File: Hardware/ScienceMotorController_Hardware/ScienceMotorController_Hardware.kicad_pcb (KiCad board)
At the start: 2 copper layers, 124.5 x 104.9 mm, 109 parts, among them SW1 SW_Push, SW2 SW_Push, SW3 SW_Push, SW4 SW_Push, U1 TM4C129E_Launchpad, U2 3.3V OKI, U3 5V OKI, U4 VNH5019A_E, U5 VNH5019A_E, U6 VNH5019A_E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

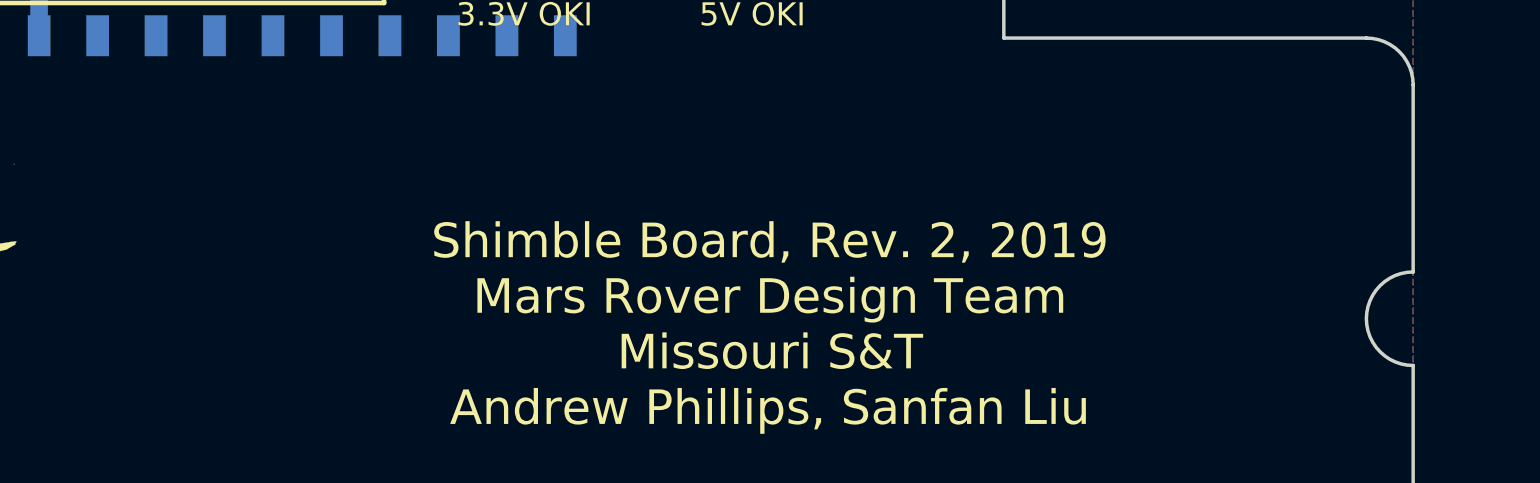
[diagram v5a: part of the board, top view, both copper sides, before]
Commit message: Fixed Silkscreen
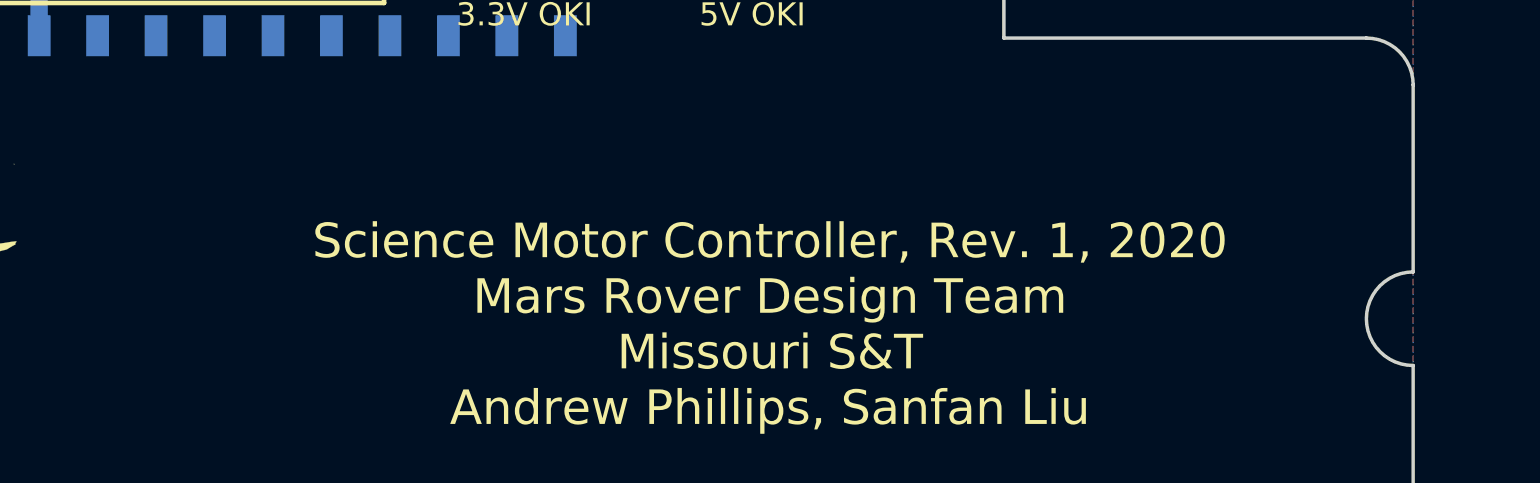
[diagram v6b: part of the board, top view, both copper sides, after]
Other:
- board text added: "Science Motor Controller, Rev. 1, 2020 Mars Rover Design Team Missouri S&T Andrew Phillips, Sanfan Liu"
- board text removed: "Shimble Board, Rev. 2, 2019 Mars Rover Design Team Missouri S&T Andrew Phillips, Sanfan Liu"

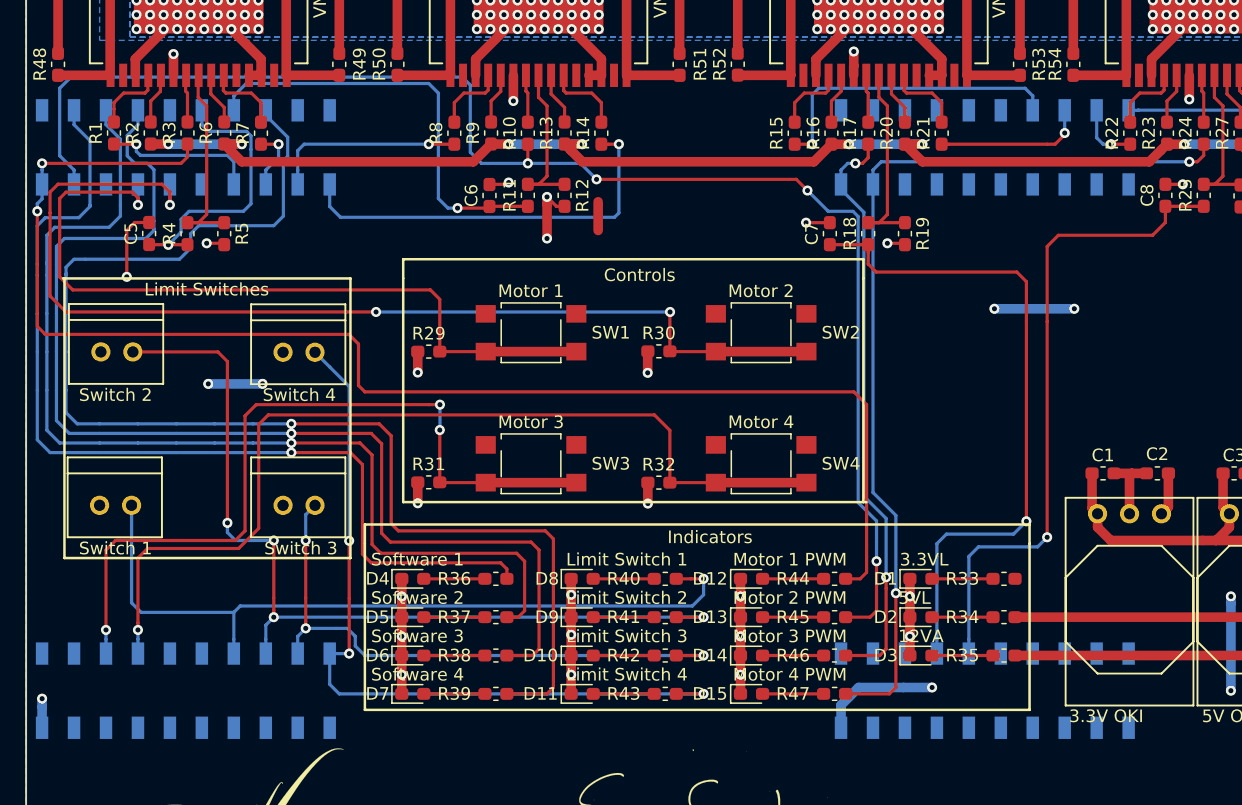
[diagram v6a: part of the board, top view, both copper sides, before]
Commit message: PDR Advice
Removed 2 limit switches & relocated LS LEDs, added direction switch. Also relocated LS, Control, and Indicator blocks and revamped pin assignments to optimize traces.
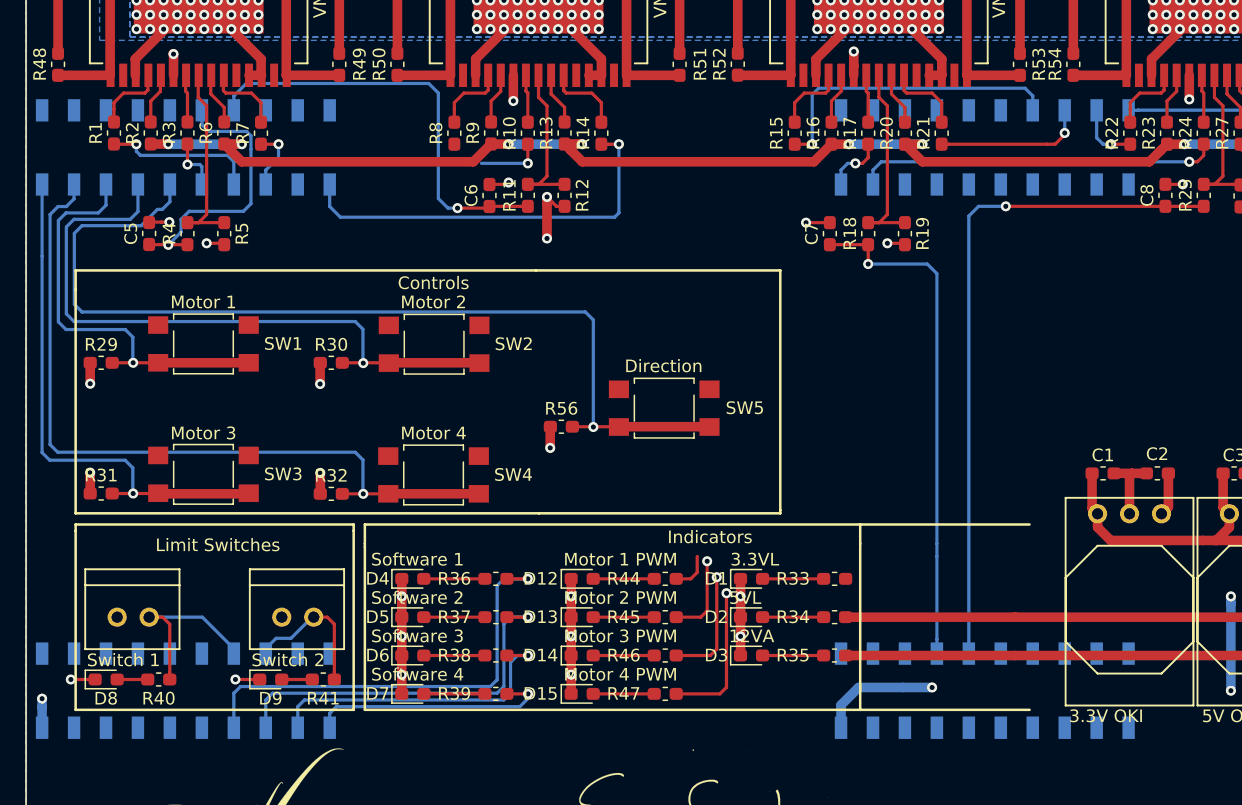
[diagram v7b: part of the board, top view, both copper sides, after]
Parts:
- removed Conn8, Conn9: Molex_SL_02, MRDT_Connectors:MOLEX_SL_02_Vertical
- removed D10: LS_3_LED, LED_SMD:LED_0603_1608Metric_Pad1.05x0.95mm_HandSolder
- removed D11: LS_4_LED, LED_SMD:LED_0603_1608Metric_Pad1.05x0.95mm_HandSolder
- removed R42, R43: 500, Resistor_SMD:R_0603_1608Metric_Pad1.05x0.95mm_HandSolder
- added R56: 500, Resistor_SMD:R_0603_1608Metric_Pad1.05x0.95mm_HandSolder, F.Cu at (81.2, 115.9)
- added SW5: SW_Push, Button_Switch_SMD:SW_SPST_TL3305A, F.Cu at (89.3, 114.5)
- moved R40 41.0 mm to (49.1, 136.0)
- moved D8 38.7 mm to (45.0, 136.0)
- moved R41 27.6 mm to (62.2, 136.0)
- moved R30 26.1 mm to (62.9, 110.8)
- moved SW4 26.1 mm to (71.0, 119.8)
- moved R32 26.1 mm to (62.9, 121.3)
- moved R29 26.1 mm to (44.6, 110.8)
- moved R31 26.1 mm to (44.6, 121.2)
- moved SW1 26.1 mm to (52.7, 109.3)
- moved SW3 26.0 mm to (52.7, 119.7)
- moved SW2 26.0 mm to (71.0, 109.4)
- moved Conn7 25.5 mm to (60.2, 131.1)
- moved D9 25.2 mm to (58.1, 136.0)
- moved D12 13.5 mm to (82.8, 128.0)
- moved D13 13.5 mm to (82.8, 131.1)
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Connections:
- U1 pad PB2: Net-(U1-PadPB2) -> SW_IND_3
- U1 pad PB3: Net-(U1-PadPB3) -> SW_IND_4
- U1 pad PC7: Net-(U1-PadPC7) -> SW_IND_2
- U1 pad PD3: Net-(U1-PadPD3) -> SW_IND_1
- U1 pad PE0: MSW_3 -> Net-(U1-PadPE0)
- U1 pad PE1: MSW_4 -> Net-(U1-PadPE1)
- U1 pad PF1: M1_PWM -> MSW_3
- U1 pad PF2: M2_PWM -> MSW_4
- U1 pad PF3: Net-(U1-PadPF3) -> MSW_1
- U1 pad PG0: MSW_1 -> MSW_2
- U1 pad PH2: SW_IND_2 -> Net-(U1-PadPH2)
- U1 pad PH3: SW_IND_3 -> Net-(U1-PadPH3)
- U1 pad PL4: MSW_2 -> MSW_5
- U1 pad PL5: Net-(U1-PadPL5) -> M1_PWM
- U1 pad PM3: SW_IND_1 -> Net-(U1-PadPM3)
- U1 pad PM4: LS_3 -> Net-(U1-PadPM4)
- U1 pad PM5: LS_4 -> Net-(U1-PadPM5)
- U1 pad PN2: SW_IND_4 -> Net-(U1-PadPN2)
- U1 pad PP2: Net-(U1-PadPP2) -> M2_PWM
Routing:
- net M1_PWM: track 111.5 -> 7.41 mm, vias 2 -> 1
- net M2_PWM: track 115.8 -> 11.8 mm, vias 4 -> 2
- net SW_IND_4: track 103.2 -> 19.4 mm
- net MSW_5: track 0.00 -> 76.9 mm, vias 0 -> 1
- net SW_IND_3: track 90.9 -> 24.8 mm
- net LS_4: track 61.3 -> 0.00 mm, vias 3 -> 0
- net LS_2: track 71.0 -> 11.5 mm, vias 4 -> 0
- net SW_IND_2: track 82.8 -> 30.3 mm
- net LS_3: track 47.7 -> 0.00 mm, vias 3 -> 0
- net LS_1: track 60.8 -> 14.4 mm, vias 1 -> 0
- net SW_IND_1: track 76.5 -> 35.9 mm
- net M4_PWM: track 73.7 -> 40.5 mm
- net M3_PWM: track 46.6 -> 14.3 mm
- net MSW_2: track 84.7 -> 52.9 mm, vias 3 -> 1
- net MSW_1: track 61.0 -> 33.2 mm
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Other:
- board text added: "Direction"
- board text removed: "Limit Switch 1"
- board text removed: "Limit Switch 2"
- board text removed: "Limit Switch 3"
- board text removed: "Limit Switch 4"
- board text removed: "Switch 3"
- board text removed: "Switch 4"

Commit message: Finished Traces
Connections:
- U1 pad PL2: M2_IN_A -> M2_PWM
- U1 pad PP2: M2_PWM -> M2_IN_A
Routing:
- net M1_PWM: track 7.41 -> 75.0 mm, vias 1 -> 4
- net M2_PWM: track 11.8 -> 73.7 mm, vias 2 -> 5
- net M4_PWM: track 40.5 -> 83.1 mm
- net M3_PWM: track 14.3 -> 54.1 mm
- net M2_IN_A: track 0.00 -> 12.6 mm, vias 0 -> 1
- net +3V3: track 23.3 -> 15.8 mm, vias 4 -> 2
